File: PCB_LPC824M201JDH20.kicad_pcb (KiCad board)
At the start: 2 copper layers, 15.2 x 25.4 mm, 10 parts, among them J1 Conn_01x10, J2 Conn_01x10, U1 LPC824M201JDH20

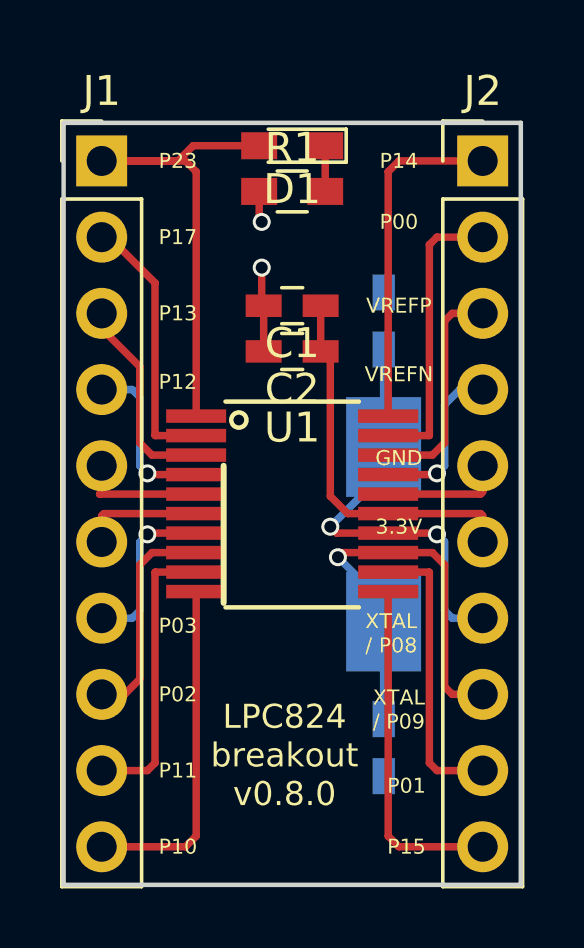
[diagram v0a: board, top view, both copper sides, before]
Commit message: fix front silkscreen
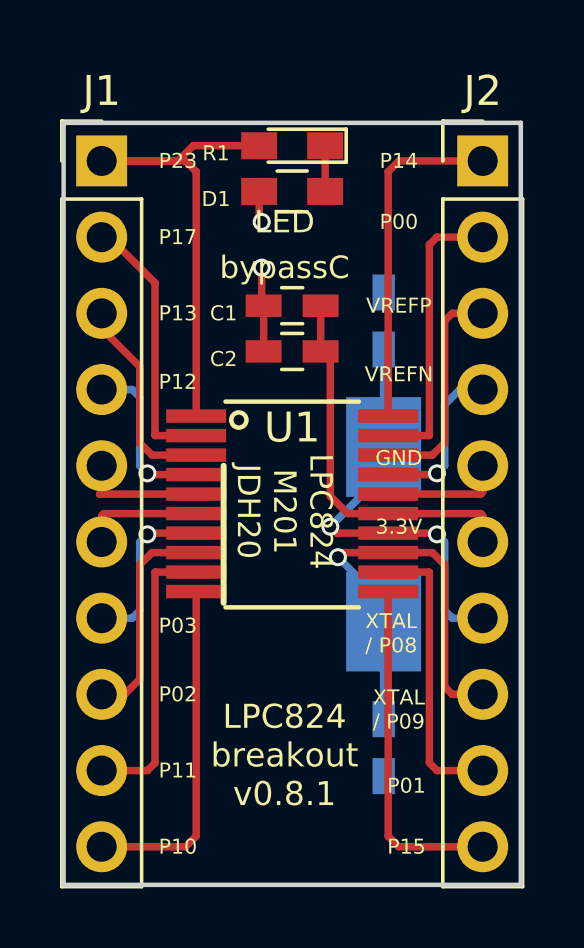
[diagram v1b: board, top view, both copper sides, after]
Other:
- board text added: "LED"
- board text added: "LPC824 M201 JDH20"
- board text added: "LPC824 breakout v0.8.1"
- board text added: "bypassC"
- board text removed: "LPC824 breakout v0.8.0"
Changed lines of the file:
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@@
     (links 33)
     (no_connects 1)
-    (area 137.517381 95.705 159.66262 125.125)
+    (area 140.894999 97.714999 156.285001 123.265001)
     (thickness 1.6)
-    (drawings 24)
+    (drawings 27)
     (tracks 122)
     (zones 0)
@@
     (pad_to_mask_clearance 0.2)
     (aux_axis_origin 0 0)
-    (visible_elements FFFCFF7F)
+    (visible_elements FFFEFF7F)
     (pcbplotparams
       (layerselection 0x010f0_80000001)
@@
     (tags "capacitor 0603")
     (attr smd)
-    (fp_text reference C1 (at 0 -1.25 180) (layer F.SilkS)
-      (effects (font (size 1 1) (thickness 0.15)))
+    (fp_text reference C1 (at 2.286 -0.254 180) (layer F.SilkS)
+      (effects (font (size 0.5 0.5) (thickness 0.125)))
     )
     (fp_text value C (at 0 1.5 180) (layer F.Fab)
-      (effects (font (size 1 1) (thickness 0.15)))
-    )
-    (fp_text user %R (at 0 -1.25 180) (layer F.Fab)
       (effects (font (size 1 1) (thickness 0.15)))
     )
@@
     (tags "LED 0603")
     (attr smd)
-    (fp_text reference D1 (at 0 -1.45 180) (layer F.SilkS)
-      (effects (font (size 1 1) (thickness 0.15)))
+    (fp_text reference D1 (at 2.54 -1.778 180) (layer F.SilkS)
+      (effects (font (size 0.5 0.5) (thickness 0.125)))
     )
     (fp_text value LED (at 0 1.55 180) (layer F.Fab)
@@
     (tags "resistor 0603")
     (attr smd)
-    (fp_text reference R1 (at 0 -1.45) (layer F.SilkS)
-      (effects (font (size 1 1) (thickness 0.15)))
+    (fp_text reference R1 (at -2.54 -1.27) (layer F.SilkS)
+      (effects (font (size 0.5 0.5) (thickness 0.125)))
     )
     (fp_text value R (at 0 1.55) (layer F.Fab)
@@
     (tags "capacitor 0603")
     (attr smd)
-    (fp_text reference C2 (at 0 -1.25 180) (layer F.SilkS)
-      (effects (font (size 1 1) (thickness 0.15)))
+    (fp_text reference C2 (at 2.286 -0.254 180) (layer F.SilkS)
+      (effects (font (size 0.5 0.5) (thickness 0.125)))
     )
     (fp_text value C (at 0 1.5 180) (layer F.Fab)
-      (effects (font (size 1 1) (thickness 0.15)))
-    )
-    (fp_text user %R (at 0 -1.25 180) (layer F.Fab)
       (effects (font (size 1 1) (thickness 0.15)))
     )
@@
     )
   )
+  (gr_text "LPC824\nM201\nJDH20" (at 148.336 110.744 270) (layer F.SilkS)
+    (effects (font (size 0.75 0.75) (thickness 0.1)))
+  )
+  (gr_text LED (at 148.336 101.092) (layer F.SilkS)
+    (effects (font (size 0.75 0.75) (thickness 0.1)))
+  )
+  (gr_text bypassC (at 148.336 102.616) (layer F.SilkS)
+    (effects (font (size 0.75 0.75) (thickness 0.1)))
+  )
   (gr_text "XTAL \n/ P08\n" (at 151.892 114.808) (layer F.SilkS)
     (effects (font (size 0.5 0.5) (thickness 0.1)))
@@
   (gr_line (start 140.97 97.79) (end 156.21 97.79) (angle 90) (layer Edge.Cuts) (width 0.15))
   (gr_line (start 146.304 109.22) (end 146.304 113.792) (angle 90) (layer F.SilkS) (width 0.2))
-  (gr_text "LPC824\nbreakout\nv0.8.0" (at 148.336 118.872) (layer F.SilkS)
+  (gr_text "LPC824\nbreakout\nv0.8.1" (at 148.336 118.872) (layer F.SilkS)
     (effects (font (size 0.8 0.8) (thickness 0.1)))
   )

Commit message: fix back silkscreen, add URL to github repo
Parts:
- renumbered 12MHz1 to Crystal
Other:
- board text added: "https://github.com/jdesbonnet/ PCB_LPC824M201JDH20_breakout"
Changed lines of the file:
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@@
     (area 140.894999 97.714999 156.285001 123.265001)
     (thickness 1.6)
-    (drawings 27)
+    (drawings 28)
     (tracks 122)
     (zones 0)
@@
   (page A4)
   (layers
-    (0 F.Cu signal)
-    (31 B.Cu signal)
+    (0 F.Cu signal hide)
+    (31 B.Cu signal hide)
     (32 B.Adhes user hide)
     (33 F.Adhes user hide)
@@
     (35 F.Paste user hide)
     (36 B.SilkS user)
-    (37 F.SilkS user)
+    (37 F.SilkS user hide)
     (38 B.Mask user)
     (39 F.Mask user)
@@
     (tags "capacitor 0603")
     (attr smd)
-    (fp_text reference C4 (at 0 1.25 90) (layer B.SilkS)
+    (fp_text reference C4 (at 0 -1.524 90) (layer B.SilkS)
       (effects (font (size 1 1) (thickness 0.15)) (justify mirror))
     )
@@
     (tags "SMD SMT crystal hand-soldering")
     (attr smd)
-    (fp_text reference 12MHz1 (at 0 2.95 90) (layer B.SilkS)
+    (fp_text reference Crystal (at -0.254 -3.048 90) (layer B.SilkS)
       (effects (font (size 1 1) (thickness 0.15)) (justify mirror))
     )
@@
     )
   )
+  (gr_text "https://github.com/jdesbonnet/\nPCB_LPC824M201JDH20_breakout" (at 145.542 110.49 90) (layer B.SilkS)
+    (effects (font (size 0.75 0.75) (thickness 0.15)) (justify mirror))
+  )
   (gr_text "LPC824\nM201\nJDH20" (at 148.336 110.744 270) (layer F.SilkS)
